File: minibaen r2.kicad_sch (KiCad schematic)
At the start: 131 parts, among them J1 USB_C_Receptacle_USB2.0, Q1 2N7002, SW1 MX_SW_solder, SW10 MX_SW_solder, SW11 MX_SW_solder, SW12 MX_SW_solder, SW13 MX_SW_solder, SW14 MX_SW_solder, SW15 MX_SW_solder, SW16 MX_SW_solder, SW17 MX_SW_solder, SW18 MX_SW_solder, SW19 MX_SW_solder, SW2 MX_SW_solder, SW20 MX_SW_solder, SW21 MX_SW_solder, SW22 MX_SW_solder, SW23 MX_SW_solder, SW24 MX_SW_solder, SW25 MX_SW_solder, SW26 MX_SW_solder, SW27 MX_SW_solder, SW28 MX_SW_solder, SW29 MX_SW_solder, SW3 MX_SW_solder, SW30 MX_SW_solder, SW31 MX_SW_solder, SW32 MX_SW_solder, SW33 MX_SW_solder, SW34 MX_SW_solder, SW35 MX_SW_solder, SW36 MX_SW_solder, SW37 MX_SW_solder, SW38 MX_SW_solder, SW39 MX_SW_solder, SW4 MX_SW_solder, SW40 MX_SW_solder, SW41 MX_SW_solder, SW42 MX_SW_solder, SW43 MX_SW_solder, SW44 MX_SW_solder, SW45 MX_SW_solder, SW46 SW_Push, SW47 MX_SW_solder, SW48 MX_SW_solder, SW49 MX_SW_solder, SW5 MX_SW_solder, SW51 MX_SW_solder, SW52 MX_SW_solder, SW53 MX_SW_solder, SW54 MX_SW_solder, SW6 MX_SW_solder, SW7 MX_SW_solder, SW8 MX_SW_solder, SW9 MX_SW_solder, U3 SRV05-4, U4 XC6206PxxxMR, U5 STM32F072C8Tx

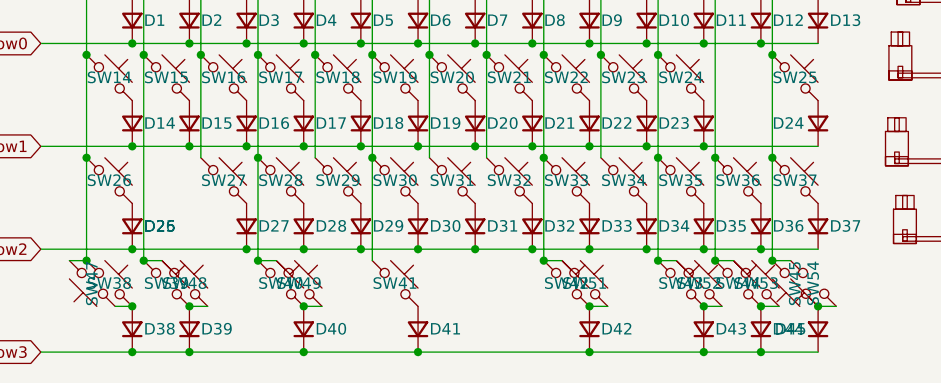
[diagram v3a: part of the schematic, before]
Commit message: fix 3v3 routing, add firmware
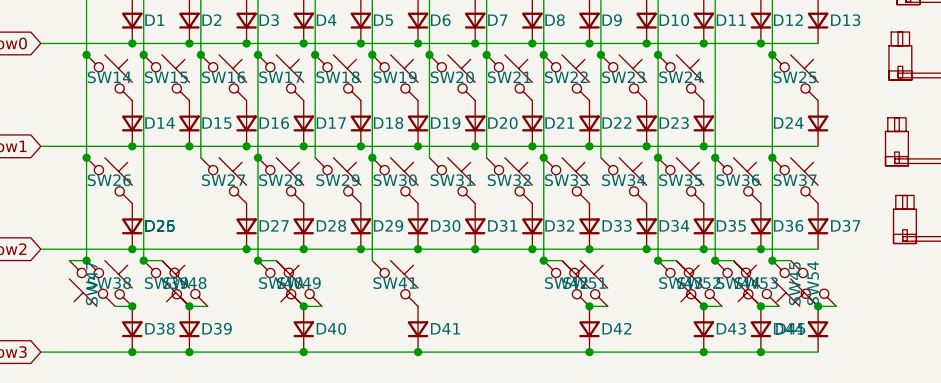
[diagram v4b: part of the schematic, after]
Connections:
- net col1: now also SW48.2; no longer SW48.1
- net col10: now also SW52.2; no longer SW52.1
- net col11: now also SW53.2; no longer SW53.1
- net col3: now also SW49.2; no longer SW49.1
- net at D39.2 (A), SW39.2: now also SW48.1; no longer SW48.2
- net at D44.2 (A), SW44.2: now also SW53.1; no longer SW53.2
- net at D40.2 (A), SW40.2: now also SW49.1; no longer SW49.2
- net at D43.2 (A), SW43.2: now also SW52.1; no longer SW52.2
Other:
- moved on the sheet: SW48, SW49, SW52, SW53
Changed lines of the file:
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@@
     (stroke (width 0) (type default))
   )
+  (wire (pts (xy 122.174 168.91) (xy 124.206 168.91))
+    (stroke (width 0) (type default))
+  )
   (polyline (pts (xy 113.792 50.038) (xy 68.072 50.038))
     (stroke (width 0) (type default))
@@
     (stroke (width 0) (type default))
   )
-  (wire (pts (xy 122.174 168.91) (xy 124.206 168.91))
-    (stroke (width 0) (type default))
-  )
   (polyline (pts (xy 176.022 62.738) (xy 176.022 57.658))
     (stroke (width 0) (type default))
@@
     (stroke (width 0) (type default))
   )
-  (wire (pts (xy 128.524 168.91) (xy 130.556 168.91))
-    (stroke (width 0) (type default))
-  )
   (wire (pts (xy 122.682 107.188) (xy 126.492 107.188))
     (stroke (width 0) (type default))
@@
     (stroke (width 0) (type default))
   )
+  (wire (pts (xy 128.524 168.91) (xy 130.556 168.91))
+    (stroke (width 0) (type default))
+  )
   (polyline (pts (xy 68.072 77.978) (xy 113.792 77.978))
     (stroke (width 0) (type default))
@@
     )
   )
-  (symbol (lib_id "marbastlib-mx:MX_SW_solder") (at 63.246 171.45 0) (unit 1)
+  (symbol (lib_id "marbastlib-mx:MX_SW_solder") (at 63.246 171.45 180) (unit 1)
     (in_bom yes) (on_board yes) (dnp no)
     (property "Reference" "SW48" (at 63.246 171.45 0)
       (effects (font (size 1.27 1.27)))
     )
-    (property "Value" "MX_SW_solder" (at 63.246 167.64 0)
+    (property "Value" "MX_SW_solder" (at 63.246 175.26 0)
       (effects (font (size 1.27 1.27)) hide)
     )
@@
     )
   )
-  (symbol (lib_id "marbastlib-mx:MX_SW_solder") (at 126.746 171.45 0) (unit 1)
+  (symbol (lib_id "marbastlib-mx:MX_SW_solder") (at 126.746 171.45 180) (unit 1)
     (in_bom yes) (on_board yes) (dnp no)
     (property "Reference" "SW53" (at 126.746 171.45 0)
       (effects (font (size 1.27 1.27)))
     )
-    (property "Value" "MX_SW_solder" (at 126.746 167.64 0)
+    (property "Value" "MX_SW_solder" (at 126.746 175.26 0)
       (effects (font (size 1.27 1.27)) hide)
     )
@@
     )
   )
-  (symbol (lib_id "marbastlib-mx:MX_SW_solder") (at 120.396 171.45 0) (unit 1)
+  (symbol (lib_id "marbastlib-mx:MX_SW_solder") (at 120.396 171.45 180) (unit 1)
     (in_bom yes) (on_board yes) (dnp no)
     (property "Reference" "SW52" (at 120.396 171.45 0)
       (effects (font (size 1.27 1.27)))
     )
-    (property "Value" "MX_SW_solder" (at 120.396 167.64 0)
+    (property "Value" "MX_SW_solder" (at 120.396 175.26 0)
       (effects (font (size 1.27 1.27)) hide)
     )
@@
     )
   )
-  (symbol (lib_id "marbastlib-mx:MX_SW_solder") (at 75.946 171.45 0) (unit 1)
+  (symbol (lib_id "marbastlib-mx:MX_SW_solder") (at 75.946 171.45 180) (unit 1)
     (in_bom yes) (on_board yes) (dnp no)
     (property "Reference" "SW49" (at 75.946 171.45 0)
       (effects (font (size 1.27 1.27)))
     )
-    (property "Value" "MX_SW_solder" (at 75.946 167.64 0)
+    (property "Value" "MX_SW_solder" (at 75.946 175.26 0)
       (effects (font (size 1.27 1.27)) hide)
     )

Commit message: updates
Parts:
- removed S5: MX_stab, marbastlib-mx:STAB_MX_2u, symbol marbastlib-mx:MX_stab
- removed SW47, SW49, SW52, SW54: MX_SW_solder, marbastlib-mx:SW_MX_1.5u, symbol marbastlib-mx:MX_SW_solder
- removed SW48, SW51, SW53: MX_SW_solder, marbastlib-mx:SW_MX_1u, symbol marbastlib-mx:MX_SW_solder
- removed U3: SRV05-4, marbastlib-various:SOT-23-6-routable, symbol Power_Protection:SRV05-4
- added D94: PRTR5V0U2X, Package_TO_SOT_SMD:SOT-143, symbol Power_Protection:PRTR5V0U2X
- added H6: MountingHole, MountingHole:MountingHole_2.2mm_M2_DIN965_Pad, symbol Mechanical:MountingHole_Pad
- added SW50, SW55, SW56, SW57: MX_SW_solder, marbastlib-mx:SW_MX_1u, symbol marbastlib-mx:MX_SW_solder
- S4: footprint marbastlib-mx:STAB_MX_2.75u -> marbastlib-mx:STAB_MX_6.25u
- SW37: footprint marbastlib-mx:SW_MX_1.25u -> marbastlib-mx:SW_MX_1u
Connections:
- net D+: now also D94.2 (I/O1)
- net D-: now also D94.3 (I/O2)
- net GND: now also D94.1 (GND), H6.1
- net VBUS: now also D94.4 (VCC)
- net col0: now also U5.21 (PB10); no longer U5.18 (PB0)
- net col1: now also U5.18 (PB0); no longer SW39.1, U5.17 (PA7)
- net col10: now also SW43.2, SW55.1; no longer SW43.1
- net col11: now also U5.13 (PA3), SW56.1; no longer U5.37 (PA14)
- net col12: now also U5.45 (PB8), SW57.1; no longer U5.46 (PB9)
- net col2: now also SW39.1, U5.17 (PA7); no longer U5.16 (PA6)
- net col3: now also U5.16 (PA6); no longer U5.15 (PA5)
- net col4: now also U5.15 (PA5); no longer U5.14 (PA4)
- net col5: now also U5.14 (PA4); no longer U5.13 (PA3)
- net col8: now also SW50.1
- net row0: now also U5.39 (PB3); no longer U5.38 (PA15)
- net row1: now also U5.22 (PB11); no longer U5.41 (PB5)
- net row2: now also U5.19 (PB1); no longer U5.40 (PB4)
- net row3: now also U5.20 (PB2); no longer U5.39 (PB3)
- net at D45.2 (A), SW45.2: now also SW57.2
- net at D42.2 (A), SW42.2: now also SW50.2
- net at D44.2 (A), SW44.2: now also SW56.2
- net at D43.2 (A): now also SW43.1, SW55.2; no longer SW43.2
- no-connect marks 4 -> 9
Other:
- moved on the sheet: D39, SW39, SW43

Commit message: idk
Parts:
- removed SW46: SW_Push, Button_Switch_SMD:SW_SPST_TL3342, symbol Switch:SW_Push
- removed SW50, SW55, SW56, SW57: MX_SW_solder, marbastlib-mx:SW_MX_1u, symbol marbastlib-mx:MX_SW_solder
- added SW46, SW47, SW49: MX_SW_solder, marbastlib-mx:SW_MX_1u, symbol marbastlib-mx:MX_SW_solder
- added SW48: MX_SW_solder, marbastlib-mx:SW_MX_1.25u, symbol marbastlib-mx:MX_SW_solder
- added SW50: SW_Push, Button_Switch_SMD:SW_SPST_TL3342, symbol Switch:SW_Push
- SW43, SW45: footprint marbastlib-mx:SW_MX_1.25u -> marbastlib-mx:SW_MX_1u
- SW44: footprint marbastlib-mx:SW_MX_1u -> marbastlib-mx:SW_MX_1.25u
- renumbered C8 to C1, C17 to C10, C18 to C11, C19 to C12, C9 to C2, C10 to C3, C11 to C4, C12 to C5, C13 to C6, C14 to C7, C15 to C8, C16 to C9, R11 to R3, R12 to R4, U5 to U1, U4 to U2
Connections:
- net +3V3: now also SW50.2
- net BOOT0: now also SW50.1
- net col10: now also SW44.2, SW45.1; no longer SW43.2
- net col11: now also SW46.1, SW47.2; no longer SW44.1
- net col12: now also SW48.1, SW49.1; no longer SW45.1
- net col8: now also SW43.1
- net at D45.2 (A): now also SW48.2, SW49.2; no longer SW45.2
- net at D42.2 (A), SW42.2: now also SW43.2
- net at D44.2 (A): now also SW46.2, SW47.1; no longer SW44.2
- net at D43.2 (A): now also SW44.1, SW45.2; no longer SW43.1
